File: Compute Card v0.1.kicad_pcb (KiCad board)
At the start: 4 copper layers, 35.9 x 55.4 mm, 3 parts, among them J1 Bus_PCI_Express_x1, U1 PI7C9X440SLBFDE

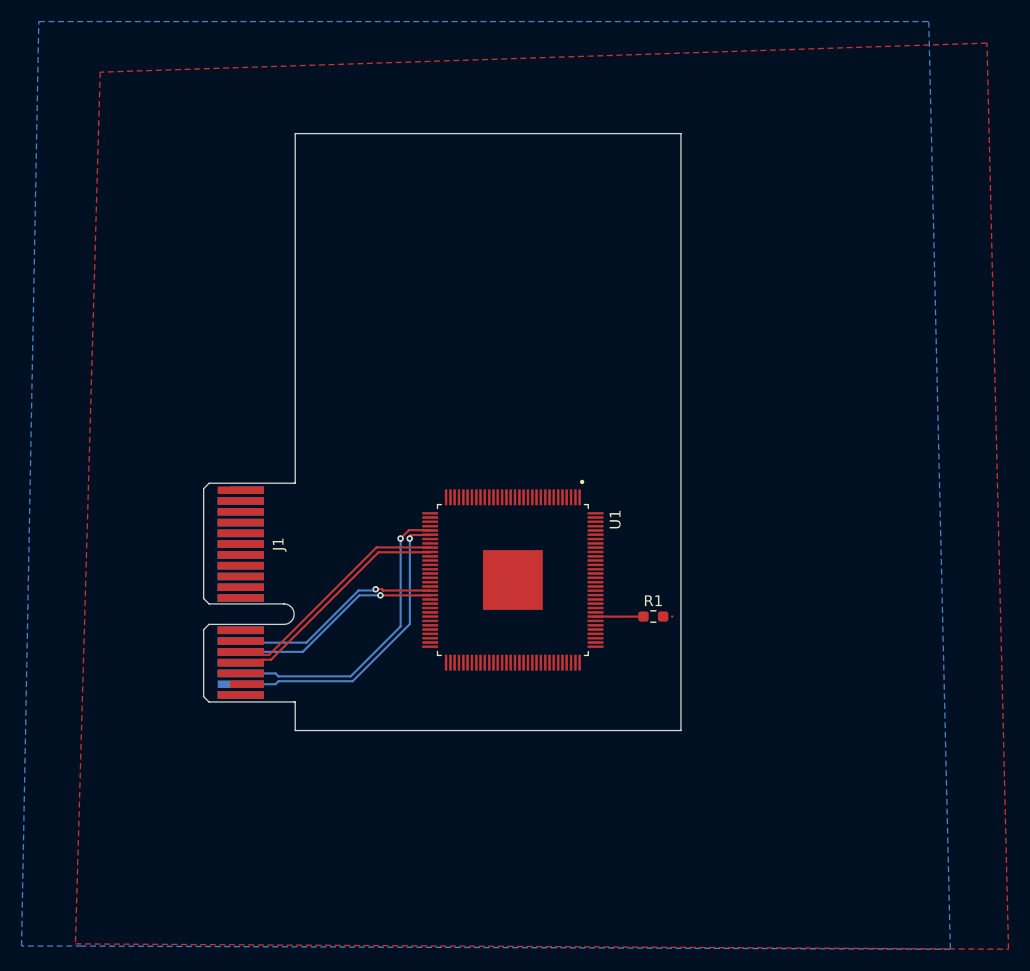
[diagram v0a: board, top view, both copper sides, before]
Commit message: Placed 1V0 parts
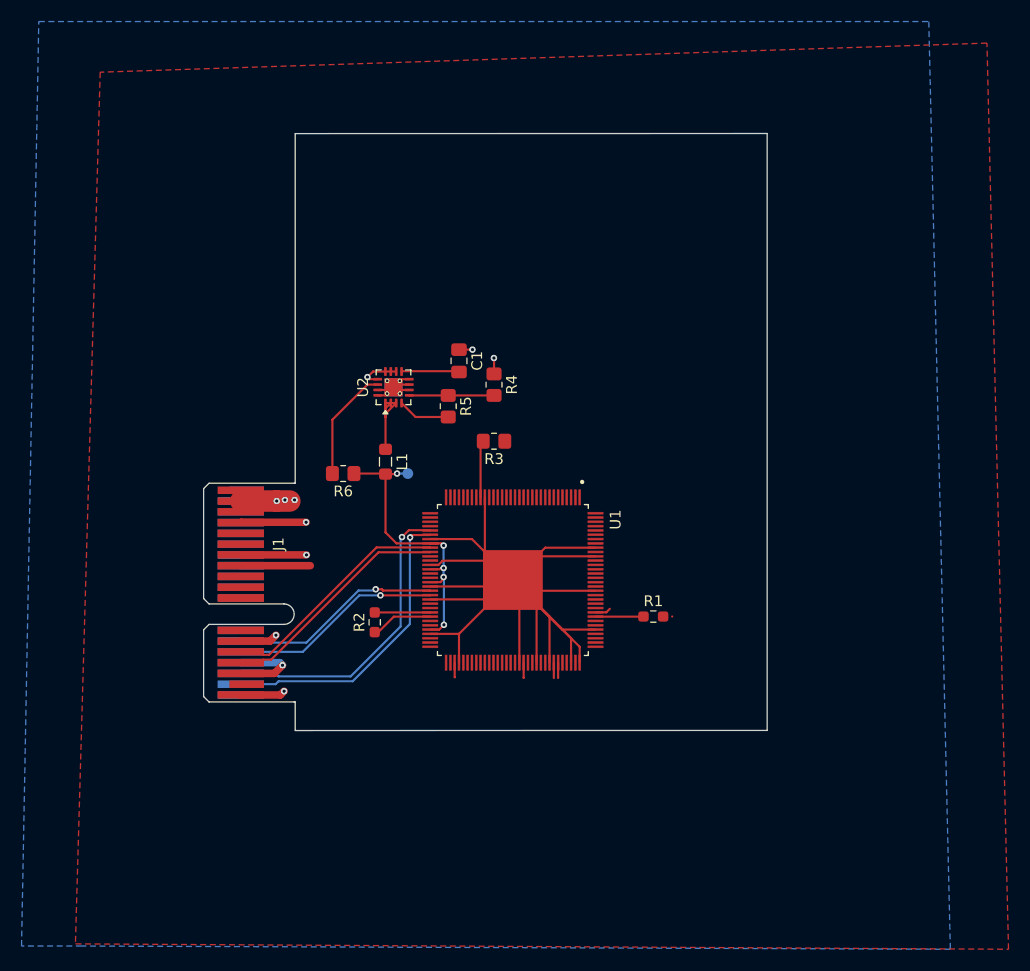
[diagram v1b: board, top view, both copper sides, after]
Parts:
- added C1: 0.1µF, Capacitor_SMD:C_0805_2012Metric_Pad1.18x1.45mm_HandSolder, F.Cu at (51.5, 63.3)
- added L1: 2.2µH, Inductor_SMD:L_0805_2012Metric_Pad1.05x1.20mm_HandSolder, F.Cu at (44.7, 72.7)
- added R2: 1.43kΩ, Resistor_SMD:R_0603_1608Metric_Pad0.98x0.95mm_HandSolder, F.Cu at (43.7, 87.6)
- added R3: 4.7kΩ, Resistor_SMD:R_0805_2012Metric_Pad1.20x1.40mm_HandSolder, F.Cu at (54.8, 70.8)
- added R4: 100kΩ, Resistor_SMD:R_0805_2012Metric_Pad1.20x1.40mm_HandSolder, F.Cu at (54.8, 65.5)
- added R5: 24.9kΩ, Resistor_SMD:R_0805_2012Metric_Pad1.20x1.40mm_HandSolder, F.Cu at (50.5, 67.5)
- added R6: 100kΩ, Resistor_SMD:R_0805_2012Metric_Pad1.20x1.40mm_HandSolder, F.Cu at (40.8, 73.8)
- added TP1: TestPoint, TestPoint:TestPoint_Pad_D1.0mm, B.Cu at (46.8, 73.8)
- added U2: TPS62130A, Package_DFN_QFN:VQFN-16-1EP_3x3mm_P0.5mm_EP1.68x1.68mm_ThermalVias, F.Cu at (45.4, 65.7)
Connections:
- net AVDD renamed +1V0
- U1 pad 105: VDDR -> +3V3
- U1 pad 112: VDDR -> +3V3
- U1 pad 115: VDDA -> +3V3
- U1 pad 121: VDDA -> +3V3
- U1 pad 122: VDDA -> +3V3
- U1 pad 128: VDDA -> +3V3
- U1 pad 24: unconnected-(U1-MAIN_DETECT-Pad24) -> Net-(U1-MAIN_DETECT)
- U1 pad 33: VDDR -> +3V3
- U1 pad 54: unconnected-(U1-AVDDH-Pad54) -> 3V3A
- U1 pad 56: unconnected-(U1-REXT_GND-Pad56) -> Net-(U1-REXT_GND)
- U1 pad 57: unconnected-(U1-REXT-Pad57) -> Net-(U1-REXT)
- U1 pad 67: VDDR -> +3V3
- U1 pad 8: VDDR -> +3V3
- U1 pad 83: VDDA -> +3V3
- U1 pad 90: VDDA -> +3V3
- U1 pad 91: VDDA -> +3V3
- U1 pad 97: VDDA -> +3V3
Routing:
- net VSS: track 0.00 -> 136.2 mm
- net GND: track 0.00 -> 40.8 mm, vias 0 -> 7
- net +1V0: track 0.00 -> 28.7 mm, vias 0 -> 5
- net +12V: track 0.00 -> 25.7 mm, vias 0 -> 4
- net +3V3: track 0.01 -> 13.5 mm
- net Net-(U2-VOS): track 0.00 -> 10.6 mm
- net Net-(L1-Pad1): track 0.00 -> 8.46 mm
- net Net-(U2-FB): track 0.00 -> 7.87 mm
- net Net-(U1-REXT): track 0.00 -> 5.74 mm
- net Net-(U2-SS/TR): track 0.00 -> 5.55 mm
- net Net-(U1-REXT_GND): track 0.00 -> 5.15 mm
- net Net-(U1-MAIN_DETECT): track 0.00 -> 4.96 mm
- net Net-(U2-PG): track 0.00 -> 4.87 mm
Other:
- board size 35.9 x 55.4 mm -> 43.9 x 55.4 mm

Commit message: Almost Completed PCIe Interface
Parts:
- added C2: 12pF, Capacitor_SMD:C_0603_1608Metric, F.Cu at (74.3, 92.0)
- added C3: 12pF, Capacitor_SMD:C_0603_1608Metric, F.Cu at (78.2, 82.4)
- added C4: 12pF, Capacitor_SMD:C_0603_1608Metric, F.Cu at (62.2, 58.0)
- added C5: 12pF, Capacitor_SMD:C_0603_1608Metric, F.Cu at (65.2, 70.3)
- added R10: 4.7kΩ, Resistor_SMD:R_0805_2012Metric_Pad1.20x1.40mm_HandSolder, F.Cu at (61.7, 70.8)
- added R11: 4.7kΩ, Resistor_SMD:R_0805_2012Metric_Pad1.20x1.40mm_HandSolder, F.Cu at (54.0, 96.2)
- added R12: 4.7kΩ, Resistor_SMD:R_0805_2012Metric_Pad1.20x1.40mm_HandSolder, F.Cu at (50.5, 70.8)
- added R7: 4.7kΩ, Resistor_SMD:R_0805_2012Metric_Pad1.20x1.40mm_HandSolder, F.Cu at (44.2, 96.2)
- added R8: 4.7kΩ, Resistor_SMD:R_0805_2012Metric_Pad1.20x1.40mm_HandSolder, F.Cu at (69.7, 83.0)
- added R9: 4.7kΩ, Resistor_SMD:R_0805_2012Metric_Pad1.20x1.40mm_HandSolder, F.Cu at (49.4, 96.2)
- added TP2: TestPoint, TestPoint:TestPoint_Pad_D1.0mm, B.Cu at (68.7, 93.5)
- added TP3: TestPoint, TestPoint:TestPoint_Pad_D1.0mm, B.Cu at (71.7, 91.3)
- added TP4: TestPoint, TestPoint:TestPoint_Pad_D1.0mm, B.Cu at (51.0, 71.2)
- added TP5: TestPoint, TestPoint:TestPoint_Pad_D1.0mm, B.Cu at (52.7, 79.6)
- added TP6: TestPoint, TestPoint:TestPoint_Pad_D1.0mm, B.Cu at (53.1, 71.2)
- added TP7: TestPoint, TestPoint:TestPoint_Pad_D1.0mm, B.Cu at (52.7, 77.4)
- added TP8: TestPoint, TestPoint:TestPoint_Pad_D1.0mm, B.Cu at (47.0, 70.8)
- added U3: CAT24C04C4ATR, WLCSP4_0P84X0P86_ONS:WLCSP4_0P84X0P86_ONS, F.Cu at (68.9, 90.8)
- added U4: RP2040, Package_DFN_QFN:QFN-56-1EP_7x7mm_P0.4mm_EP3.2x3.2mm_ThermalVias, F.Cu at (72.3, 63.2)
- added Y1: WE-XTAL_CFPX-104, WE-XTAL_CFPX-104:WE-XTAL_CFPX-104, F.Cu at (76.2, 87.3)
- added Y2: WE-XTAL_CFPX-104, WE-XTAL_CFPX-104:WE-XTAL_CFPX-104, F.Cu at (63.4, 64.9)
- moved R1 0.27 mm to (69.5, 86.8)
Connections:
- J1 pad B5: unconnected-(J1-SMCLK-PadB5) -> SMCLK
- J1 pad B6: unconnected-(J1-SMDAT-PadB6) -> SMDAT
- U1 pad 1: unconnected-(U1-TEST1-Pad1) -> Net-(U1-TEST1)
- U1 pad 101: VSS -> GND
- U1 pad 102: unconnected-(U1-XI-Pad102) -> Net-(U1-XI)
- U1 pad 103: unconnected-(U1-XO-Pad103) -> Net-(U1-XO)
- U1 pad 106: VSS -> GND
- U1 pad 110: VSS -> GND
- U1 pad 114: unconnected-(U1-TEST5-Pad114) -> Net-(U1-TEST5)
- U1 pad 118: VSS -> GND
- U1 pad 120: VSS -> GND
- U1 pad 123: unconnected-(U1-DM[1]-Pad123) -> USB_D-
- U1 pad 124: unconnected-(U1-DP[1]-Pad124) -> USB_D+
- U1 pad 125: VSS -> GND
- U1 pad 127: VSS -> GND
- U1 pad 129: VSS -> GND
- U1 pad 21: unconnected-(U1-SMBCLK-Pad21) -> SMCLK
- U1 pad 23: VSS -> GND
- U1 pad 25: unconnected-(U1-TDO-Pad25) -> Net-(U1-TDO)
- U1 pad 26: unconnected-(U1-TCK-Pad26) -> Net-(U1-TCK)
- U1 pad 27: unconnected-(U1-TMS-Pad27) -> Net-(U1-TMS)
- U1 pad 28: unconnected-(U1-TDI-Pad28) -> Net-(U1-TDI)
- U1 pad 29: unconnected-(U1-TRST_L-Pad29) -> Net-(U1-TRST_L)
- U1 pad 34: VSS -> GND
- U1 pad 36: VSS -> GND
- U1 pad 39: VSS -> GND
- U1 pad 45: VSS -> GND
- U1 pad 50: VSS -> GND
- U1 pad 53: VSS -> GND
- U1 pad 61: VSS -> GND
- U1 pad 64: unconnected-(U1-SMBDATA-Pad64) -> SMDAT
- U1 pad 65: unconnected-(U1-TEST3-Pad65) -> Net-(U1-TEST3)
- U1 pad 66: unconnected-(U1-TEST6-Pad66) -> Net-(U1-TEST6)
- U1 pad 68: VSS -> GND
- U1 pad 77: unconnected-(U1-TEST4-Pad77) -> Net-(U1-TEST4)
- U1 pad 82: VSS -> GND
- U1 pad 86: VSS -> GND
- U1 pad 89: VSS -> GND
- U1 pad 9: VSS -> GND
- U1 pad 94: VSS -> GND
- U1 pad 96: VSS -> GND
- U1 pad 98: unconnected-(U1-EEPD-Pad98) -> Net-(U1-EEPD)
- U1 pad 99: unconnected-(U1-EECLK-Pad99) -> Net-(U1-EECLK)
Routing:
- net VSS: track 136.2 -> 0.00 mm
- net GND: track 40.8 -> 104.1 mm, vias 7 -> 39
- net USB_D-: track 0.00 -> 27.5 mm, vias 0 -> 2
- net USB_D+: track 0.00 -> 26.5 mm, vias 0 -> 2
- net SMCLK: track 0.00 -> 25.6 mm, vias 0 -> 2
- net SMDAT: track 0.00 -> 21.6 mm, vias 0 -> 2
- net Net-(U1-XO): track 0.00 -> 17.5 mm
- net Net-(U4-XOUT): track 0.00 -> 16.7 mm, vias 0 -> 2
- net Net-(U1-XI): track 0.00 -> 13.2 mm
- net +3V3: track 13.5 -> 24.8 mm
- net Net-(U4-XIN): track 0.00 -> 10.9 mm
- net Net-(U1-EECLK): track 0.00 -> 8.87 mm, vias 0 -> 2
- net Net-(U1-TRST_L): track 0.00 -> 8.53 mm, vias 0 -> 1
- net Net-(U1-EEPD): track 0.00 -> 8.09 mm, vias 0 -> 1
- net Net-(U1-TEST3): track 0.00 -> 7.10 mm
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- added copper zone on B.Cu, net (none)
- added copper zone on In2.Cu, net (none)
- removed copper zone on B.Cu, net GND
- removed copper zone on In2.Cu, net GND

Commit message: Added RP2ß40 as Main MCU
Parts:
- added R13: 4.7kΩ, Resistor_SMD:R_0805_2012Metric_Pad1.20x1.40mm_HandSolder, F.Cu at (70.0, 73.5)
- added R14: 4.7kΩ, Resistor_SMD:R_0805_2012Metric_Pad1.20x1.40mm_HandSolder, F.Cu at (70.0, 70.5)
- added R15: 4.7kΩ, Resistor_SMD:R_0805_2012Metric_Pad1.20x1.40mm_HandSolder, F.Cu at (59.0, 58.2)
- added R16: 4.7kΩ, Resistor_SMD:R_0805_2012Metric_Pad1.20x1.40mm_HandSolder, F.Cu at (55.8, 58.2)
- added R17: 5.9kΩ, Resistor_SMD:R_0603_1608Metric, F.Cu at (73.3, 78.2)
- added R18: 137Ω, Resistor_SMD:R_1206_3216Metric, F.Cu at (77.8, 76.8)
- added TP10: TestPoint, TestPoint:TestPoint_Pad_D1.0mm, F.Cu at (75.5, 76.5)
- added TP11: TestPoint, TestPoint:TestPoint_Pad_D1.0mm, B.Cu at (67.0, 81.2)
- added TP12: TestPoint, TestPoint:TestPoint_Pad_D1.0mm, B.Cu at (62.2, 94.8)
- added TP13: TestPoint, TestPoint:TestPoint_Pad_D1.0mm, B.Cu at (59.2, 94.8)
- added TP9: TestPoint, TestPoint:TestPoint_Pad_D1.0mm, B.Cu at (58.2, 78.2)
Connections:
- U1 pad 10: unconnected-(U1-POE[1]-Pad10) -> Net-(U1-POE[1])
- U1 pad 119: unconnected-(U1-RREF[2]-Pad119) -> Net-(U1-RREF[2])
- U1 pad 126: unconnected-(U1-RREF[1]-Pad126) -> Net-(U1-RREF[1])
- U1 pad 4: unconnected-(U1-OCI[1]-Pad4) -> Net-(U1-OCI[1])
- U1 pad 5: unconnected-(U1-OCI[2]-Pad5) -> Net-(U1-OCI[2])
- U1 pad 6: unconnected-(U1-OCI[3]-Pad6) -> Net-(U1-OCI[3])
- U1 pad 7: unconnected-(U1-OCI[4]-Pad7) -> Net-(U1-OCI[4])
- U1 pad 87: unconnected-(U1-RREF[4]-Pad87) -> Net-(U1-RREF[4])
- U1 pad 95: unconnected-(U1-RREF[3]-Pad95) -> Net-(U1-RREF[3])
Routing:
- net Net-(U1-OCI[4]): track 0.00 -> 19.3 mm
- net Net-(U1-OCI[3]): track 0.00 -> 17.4 mm
- net Net-(U1-OCI[2]): track 0.00 -> 10.6 mm
- net Net-(U1-OCI[1]): track 0.00 -> 8.95 mm
- net Net-(U1-RREF[1]): track 0.00 -> 8.34 mm, vias 0 -> 2
- net Net-(R17-Pad2): track 0.00 -> 5.91 mm
- net Net-(U1-RREF[4]): track 0.00 -> 3.51 mm, vias 0 -> 1
- net Net-(U1-RREF[3]): track 0.00 -> 3.47 mm, vias 0 -> 1
- net Net-(U1-RREF[2]): track 0.00 -> 2.95 mm, vias 0 -> 1
- net Net-(U1-POE[1]): track 0.00 -> 2.64 mm, vias 0 -> 1
- net Net-(U1-TEST1): track 5.16 -> 5.20 mm, vias 0 -> 2

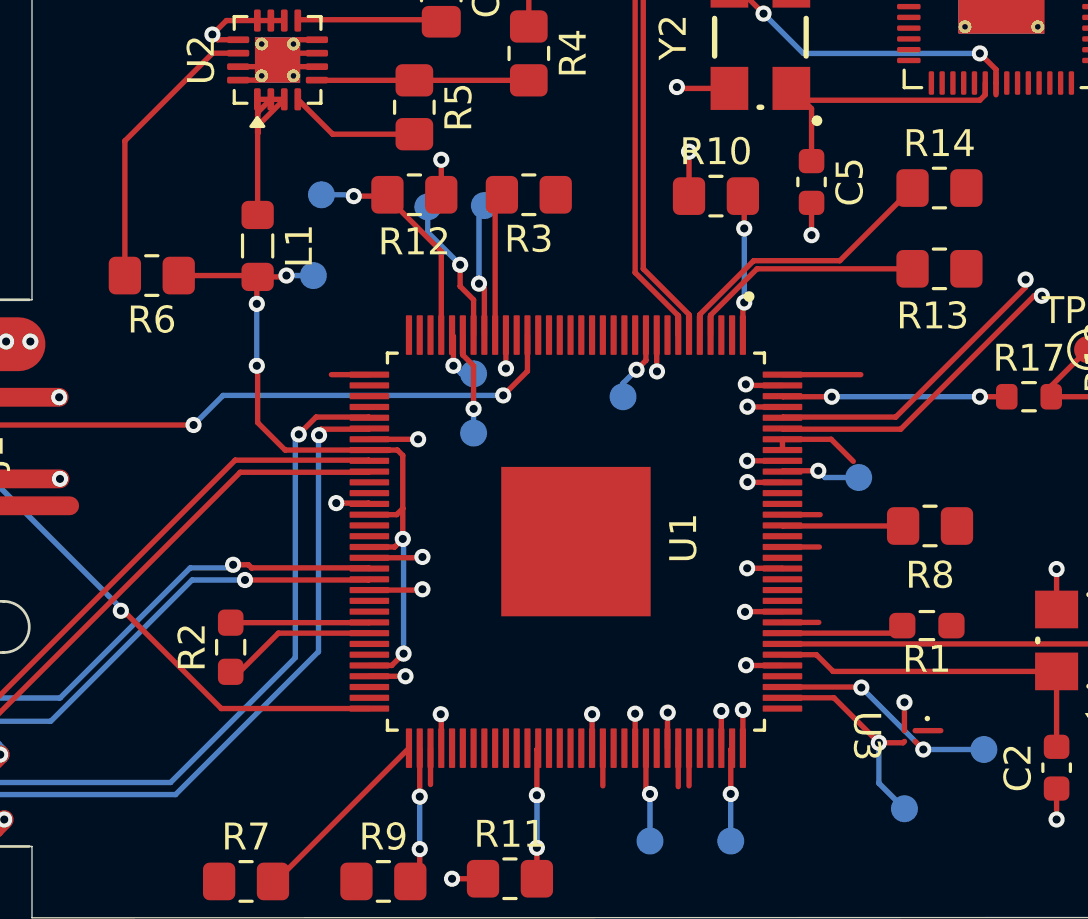
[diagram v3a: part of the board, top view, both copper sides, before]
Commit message: Completed PCIe to USB Bridge
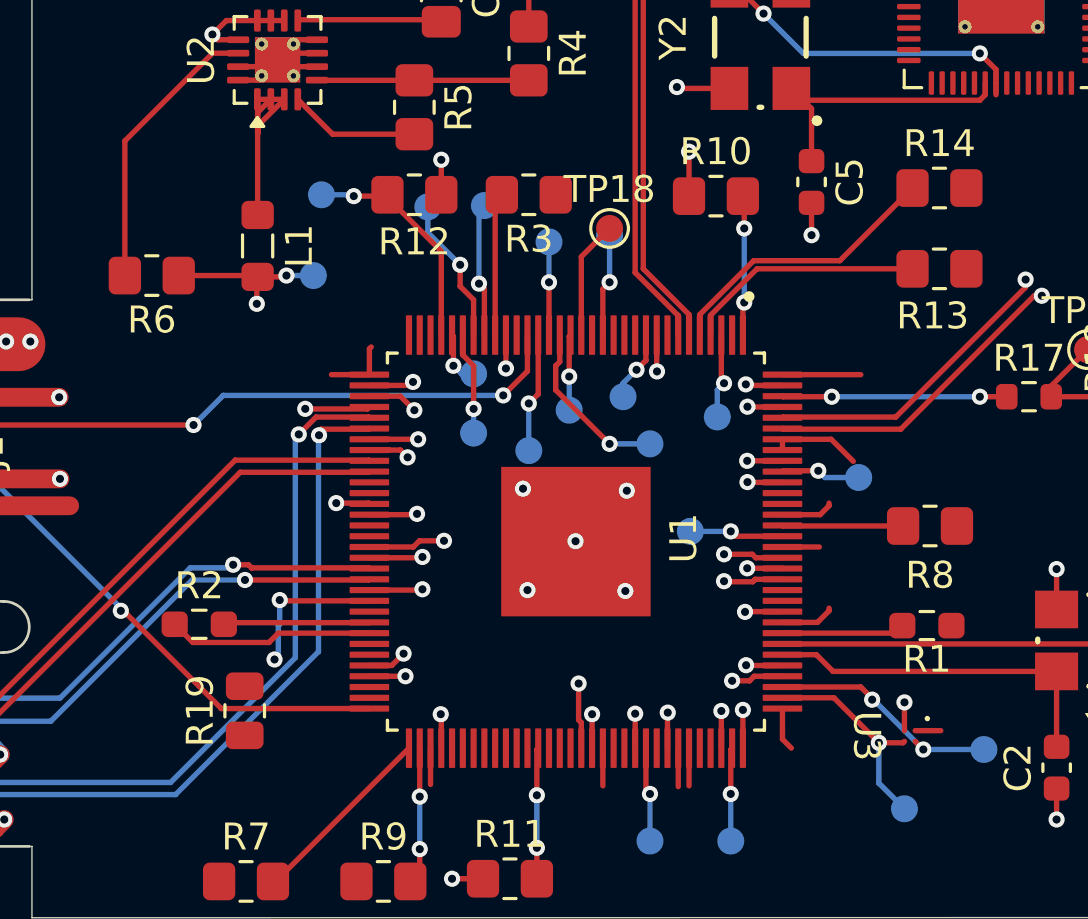
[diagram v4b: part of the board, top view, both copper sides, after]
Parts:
- added R19: 0Ω, Resistor_SMD:R_0805_2012Metric, F.Cu at (44.2, 89.9)
- added TP14: TestPoint, TestPoint:TestPoint_Pad_D1.0mm, B.Cu at (60.8, 83.2)
- added TP15: TestPoint, TestPoint:TestPoint_Pad_D1.0mm, B.Cu at (54.8, 80.2)
- added TP16: TestPoint, TestPoint:TestPoint_Pad_D1.0mm, B.Cu at (57.8, 72.2)
- added TP17: TestPoint, TestPoint:TestPoint_Pad_D1.0mm, B.Cu at (61.8, 79.0)
- added TP18: TestPoint, TestPoint:TestPoint_Pad_D1.0mm, F.Cu at (57.8, 72.0)
- added TP19: TestPoint, TestPoint:TestPoint_Pad_D1.0mm, B.Cu at (59.2, 80.0)
- added TP20: TestPoint, TestPoint:TestPoint_Pad_D1.0mm, B.Cu at (56.2, 78.8)
- added TP21: TestPoint, TestPoint:TestPoint_Pad_D1.0mm, B.Cu at (55.5, 72.5)
- moved R2 1.45 mm to (42.5, 86.7), turned to 0 degrees
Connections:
- U1 pad 100: VDDC -> +1V0
- U1 pad 109: VDDC -> +1V0
- U1 pad 111: VDDC -> +1V0
- U1 pad 113: unconnected-(U1-PME_L-Pad113) -> Net-(U1-PME_L)
- U1 pad 14: unconnected-(U1-SMI_O-Pad14) -> Net-(U1-SMI_O)
- U1 pad 16: unconnected-(U1-IRQ1_I-Pad16) -> Net-(U1-IRQ1_I)
- U1 pad 17: unconnected-(U1-IRQ12_I-Pad17) -> Net-(U1-IRQ12_I)
- U1 pad 18: unconnected-(U1-IRQ1_O-Pad18) -> Net-(U1-IRQ1_O)
- U1 pad 19: unconnected-(U1-IRQ12_O-Pad19) -> Net-(U1-IRQ12_O)
- U1 pad 20: unconnected-(U1-LEG_EMU_EN-Pad20) -> Net-(U1-LEG_EMU_EN)
- U1 pad 22: VDDC -> +1V0
- U1 pad 3: unconnected-(U1-IO_HIT_I-Pad3) -> Net-(U1-IO_HIT_I)
- U1 pad 35: VDDC -> +1V0
- U1 pad 54: 3V3A -> +3V3
- U1 pad 81: VDDC -> +1V0
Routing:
- net +3V3: track 24.8 -> 34.3 mm, vias 0 -> 2
- net Net-(U1-IRQ1_O): track 0.00 -> 6.43 mm, vias 0 -> 1
- net Net-(U1-LEG_EMU_EN): track 0.00 -> 4.43 mm, vias 0 -> 1
- net Net-(U1-IRQ1_I): track 0.00 -> 4.39 mm
- net GND: track 104.1 -> 108.2 mm, vias 39 -> 46
- net Net-(U1-SMI_O): track 0.00 -> 3.81 mm, vias 0 -> 1
- net +1V0: track 28.6 -> 25.1 mm, vias 5 -> 11
- net Net-(U1-PME_L): track 0.00 -> 3.49 mm, vias 0 -> 1
- net Net-(U1-IRQ12_O): track 0.00 -> 3.46 mm, vias 0 -> 1
- net Net-(U1-IO_HIT_I): track 0.00 -> 3.18 mm, vias 0 -> 1
- net Net-(U1-IRQ12_I): track 0.00 -> 2.81 mm, vias 0 -> 1
- net Net-(U1-REXT): track 5.74 -> 7.65 mm
- added copper zone on In2.Cu, net +1V0
